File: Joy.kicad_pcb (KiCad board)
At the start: 2 copper layers, 65 x 43 mm, 22 parts, among them IC1 MC14512BDR2G, IC2 MC14512BDR2G, J1 DB9_Male, J2 DB9_Male, J3 DB25_Male

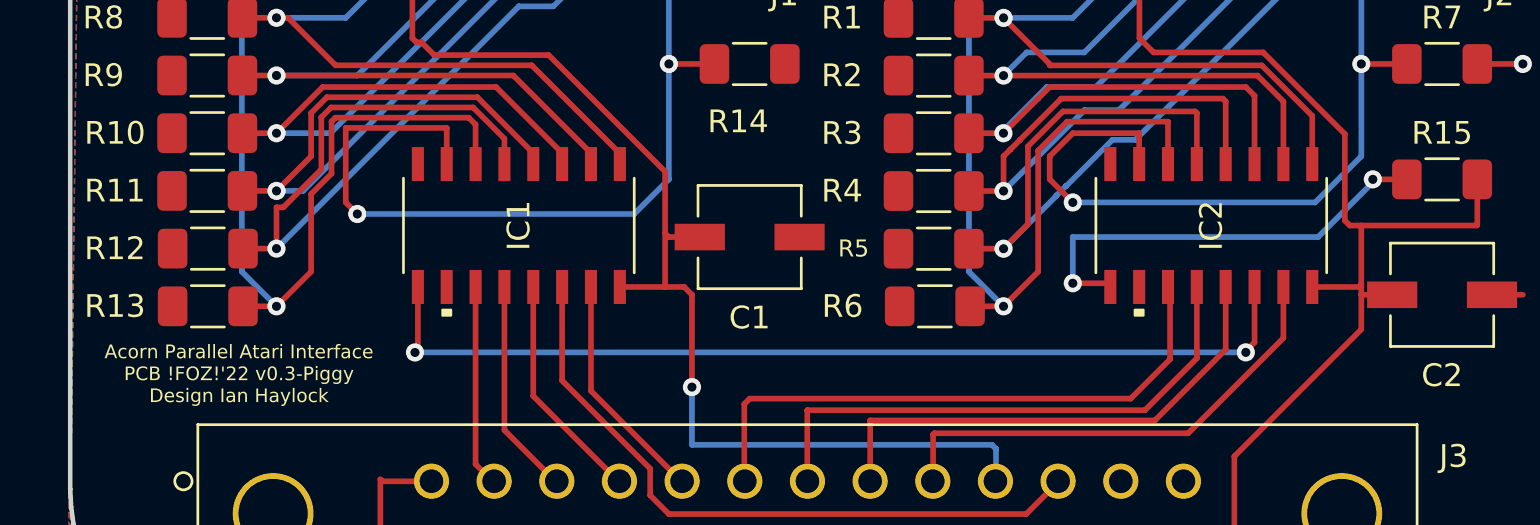
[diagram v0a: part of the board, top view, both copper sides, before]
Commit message: Added pin 1 and polarity markings to pcb and rebuilt release files for PCB v0.4
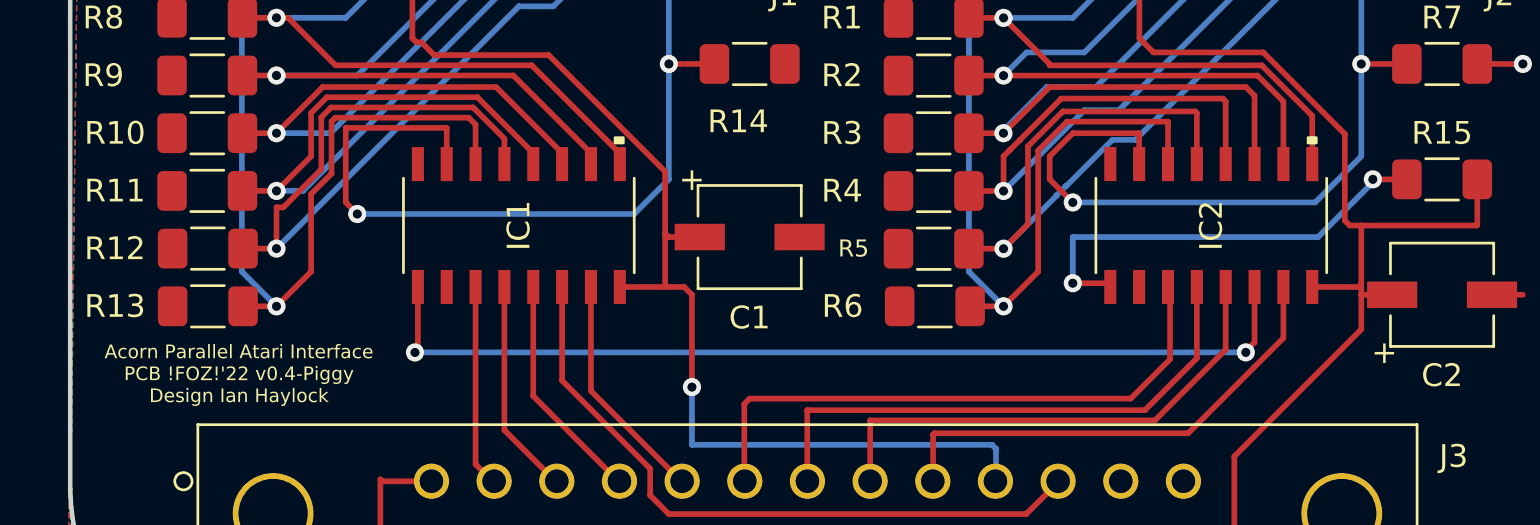
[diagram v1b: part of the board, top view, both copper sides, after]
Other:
- board text added: "Acorn Parallel Atari Interface PCB !FOZ!'22 v0.4-Piggy Design Ian Haylock"
- board text removed: "Acorn Parallel Atari Interface PCB !FOZ!'22 v0.3-Piggy Design Ian Haylock"
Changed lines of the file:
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@@
       (drillshape 0)
       (scaleselection 1)
-      (outputdirectory "")
+      (outputdirectory "release/")
     )
   )
@@
       (effects (font (size 1 1) (thickness 0.15)))
     )
+    (fp_text user "+" (at -2.54 2.54 unlocked) (layer "F.SilkS")
+      (effects (font (size 1 1) (thickness 0.15)))
+    )
     (fp_text user "*" (at 0 0) (layer "F.SilkS") hide
       (effects (font (size 1 1) (thickness 0.15)))
@@
     (fp_line (start 2.0828 -5.08) (end -2.0828 -5.08) (layer "F.SilkS") (width 0.12))
     (fp_poly (pts
-        (xy 3.9624 2.9845)
-        (xy 3.9624 3.3655)
-        (xy 3.7084 3.3655)
-        (xy 3.7084 2.9845)
+        (xy -3.623628 -4.631542)
+        (xy -3.623628 -4.250542)
+        (xy -3.877628 -4.250542)
+        (xy -3.877628 -4.631542)
       ) (layer "F.SilkS") (width 0.1) (fill solid))
     (fp_line (start 2.2098 5.207) (end -2.2098 5.207) (layer "F.CrtYd") (width 0.05))
@@
       (effects (font (size 1 1) (thickness 0.15)))
     )
+    (fp_text user "+" (at -2.54 -2.54 unlocked) (layer "F.SilkS")
+      (effects (font (size 1 1) (thickness 0.15)))
+    )
     (fp_text user "Copyright 2021 Accelerated Designs. All rights reserved." (at 0 0) (layer "Cmts.User") hide
       (effects (font (size 0.127 0.127) (thickness 0.002)))
@@
       (effects (font (size 1 1) (thickness 0.15)))
     )
+    (fp_line (start -2.2733 2.2733) (end 2.2733 2.2733) (layer "F.SilkS") (width 0.12))
     (fp_line (start -2.2733 -2.2733) (end -2.2733 -0.91694) (layer "F.SilkS") (width 0.12))
-    (fp_line (start -2.2733 2.2733) (end 2.2733 2.2733) (layer "F.SilkS") (width 0.12))
+    (fp_line (start -2.2733 0.91694) (end -2.2733 2.2733) (layer "F.SilkS") (width 0.12))
+    (fp_line (start 2.2733 2.2733) (end 2.2733 0.91694) (layer "F.SilkS") (width 0.12))
     (fp_line (start 2.2733 -0.91694) (end 2.2733 -2.2733) (layer "F.SilkS") (width 0.12))
-    (fp_line (start 2.2733 2.2733) (end 2.2733 0.91694) (layer "F.SilkS") (width 0.12))
     (fp_line (start 2.2733 -2.2733) (end -2.2733 -2.2733) (layer "F.SilkS") (width 0.12))
-    (fp_line (start -2.2733 0.91694) (end -2.2733 2.2733) (layer "F.SilkS") (width 0.12))
-    (fp_line (start -2.4003 -0.8382) (end -2.4003 -2.4003) (layer "F.CrtYd") (width 0.05))
-    (fp_line (start 2.4003 -2.4003) (end 2.4003 -0.8382) (layer "F.CrtYd") (width 0.05))
-    (fp_line (start -2.4003 0.8382) (end -3.556 0.8382) (layer "F.CrtYd") (width 0.05))
-    (fp_line (start -2.4003 2.4003) (end -2.4003 0.8382) (layer "F.CrtYd") (width 0.05))
     (fp_line (start -2.4003 -2.4003) (end 2.4003 -2.4003) (layer "F.CrtYd") (width 0.05))
     (fp_line (start -3.556 -0.8382) (end -2.4003 -0.8382) (layer "F.CrtYd") (width 0.05))
     (fp_line (start -3.556 0.8382) (end -3.556 -0.8382) (layer "F.CrtYd") (width 0.05))
+    (fp_line (start 2.4003 0.8382) (end 2.4003 2.4003) (layer "F.CrtYd") (width 0.05))
+    (fp_line (start -2.4003 0.8382) (end -3.556 0.8382) (layer "F.CrtYd") (width 0.05))
+    (fp_line (start -2.4003 2.4003) (end -2.4003 0.8382) (layer "F.CrtYd") (width 0.05))
+    (fp_line (start -2.4003 -0.8382) (end -2.4003 -2.4003) (layer "F.CrtYd") (width 0.05))
+    (fp_line (start 3.556 0.8382) (end 2.4003 0.8382) (layer "F.CrtYd") (width 0.05))
+    (fp_line (start 2.4003 -2.4003) (end 2.4003 -0.8382) (layer "F.CrtYd") (width 0.05))
+    (fp_line (start 2.4003 2.4003) (end -2.4003 2.4003) (layer "F.CrtYd") (width 0.05))
+    (fp_line (start 2.4003 -0.8382) (end 3.556 -0.8382) (layer "F.CrtYd") (width 0.05))
     (fp_line (start 3.556 -0.8382) (end 3.556 0.8382) (layer "F.CrtYd") (width 0.05))
-    (fp_line (start 2.4003 0.8382) (end 2.4003 2.4003) (layer "F.CrtYd") (width 0.05))
-    (fp_line (start 2.4003 2.4003) (end -2.4003 2.4003) (layer "F.CrtYd") (width 0.05))
-    (fp_line (start 3.556 0.8382) (end 2.4003 0.8382) (layer "F.CrtYd") (width 0.05))
-    (fp_line (start 2.4003 -0.8382) (end 3.556 -0.8382) (layer "F.CrtYd") (width 0.05))
+    (fp_line (start -2.1463 2.1463) (end 2.1463 2.1463) (layer "F.Fab") (width 0.1))
+    (fp_line (start -2.1463 -2.1463) (end -2.1463 2.1463) (layer "F.Fab") (width 0.1))
+    (fp_line (start -2.1463 1.07315) (end -1.07315 2.1463) (layer "F.Fab") (width 0.1))
     (fp_line (start 2.1463 2.1463) (end 2.1463 -2.1463) (layer "F.Fab") (width 0.1))
-    (fp_line (start -2.1463 1.07315) (end -1.07315 2.1463) (layer "F.Fab") (width 0.1))
+    (fp_line (start 2.1463 -2.1463) (end -2.1463 -2.1463) (layer "F.Fab") (width 0.1))
     (fp_line (start -2.1463 -1.07315) (end -1.07315 -2.1463) (layer "F.Fab") (width 0.1))
-    (fp_line (start 2.1463 -2.1463) (end -2.1463 -2.1463) (layer "F.Fab") (width 0.1))
-    (fp_line (start -2.1463 -2.1463) (end -2.1463 2.1463) (layer "F.Fab") (width 0.1))
-    (fp_line (start -2.1463 2.1463) (end 2.1463 2.1463) (layer "F.Fab") (width 0.1))
+    (fp_circle (center 0 0) (end 1.999996 0) (layer "F.Fab") (width 0.1) (fill none))
     (fp_circle (center -1.6383 0) (end -1.6383 0) (layer "F.Fab") (width 0.1) (fill none))
-    (fp_circle (center 0 0) (end 1.999996 0) (layer "F.Fab") (width 0.1) (fill none))
     (pad "1" smd rect (at -2.1971 0) (size 2.2098 1.1684) (layers "F.Cu" "F.Paste" "F.Mask")
       (net 28 "/ACK") (pintype "passive"))
@@
     (fp_line (start 2.0828 -5.08) (end -2.0828 -5.08) (layer "F.SilkS") (width 0.12))
     (fp_poly (pts
-        (xy 3.9624 2.9845)
-        (xy 3.9624 3.3655)
-        (xy 3.7084 3.3655)
-        (xy 3.7084 2.9845)
+        (xy -3.623628 -4.607419)
+        (xy -3.623628 -4.226419)
+        (xy -3.877628 -4.226419)
+        (xy -3.877628 -4.607419)
       ) (layer "F.SilkS") (width 0.1) (fill solid))
     (fp_line (start 3.7084 4.9657) (end 2.2098 4.9657) (layer "F.CrtYd") (width 0.05))
@@
   (gr_line (start 53.91115 72.052) (end 53.9525 72.835) (layer "Edge.Cuts") (width 0.2))
   (gr_line (start 113.1986 79.714) (end 113.9398 79.438) (layer "Edge.Cuts") (width 0.2))
-  (gr_text "Acorn Parallel Atari Interface\nPCB !FOZ!'22 v0.3-Piggy\nDesign Ian Haylock" (at 61.340715 66.979777) (layer "F.SilkS")
+  (gr_text "Acorn Parallel Atari Interface\nPCB !FOZ!'22 v0.4-Piggy\nDesign Ian Haylock" (at 61.340715 66.979777) (layer "F.SilkS")
     (effects (font (size 0.6 0.6) (thickness 0.125)))
   )
